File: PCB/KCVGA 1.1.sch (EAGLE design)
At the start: 61 parts, among them IC1 M68AW128MND, IC2 74245ADB, IC4 LD117AS12TR, IC5 LD117AS33TR, U1 XC3S50ATQ144, U2 PIC32MX250F128B_I_SS, U3 PIC32MX270F256D, X1 D-SUB15, X2 MINI-USB

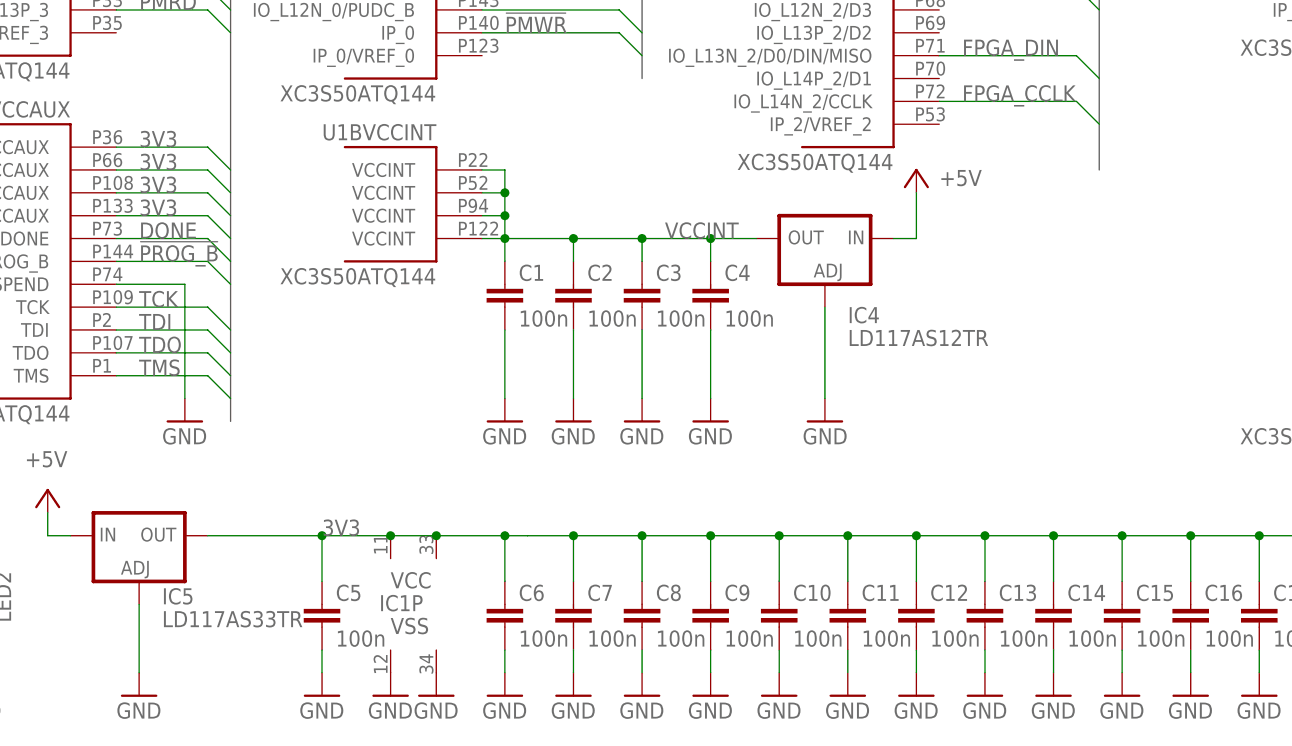
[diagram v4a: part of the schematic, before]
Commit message: added LDO output caps added Eagle3d files
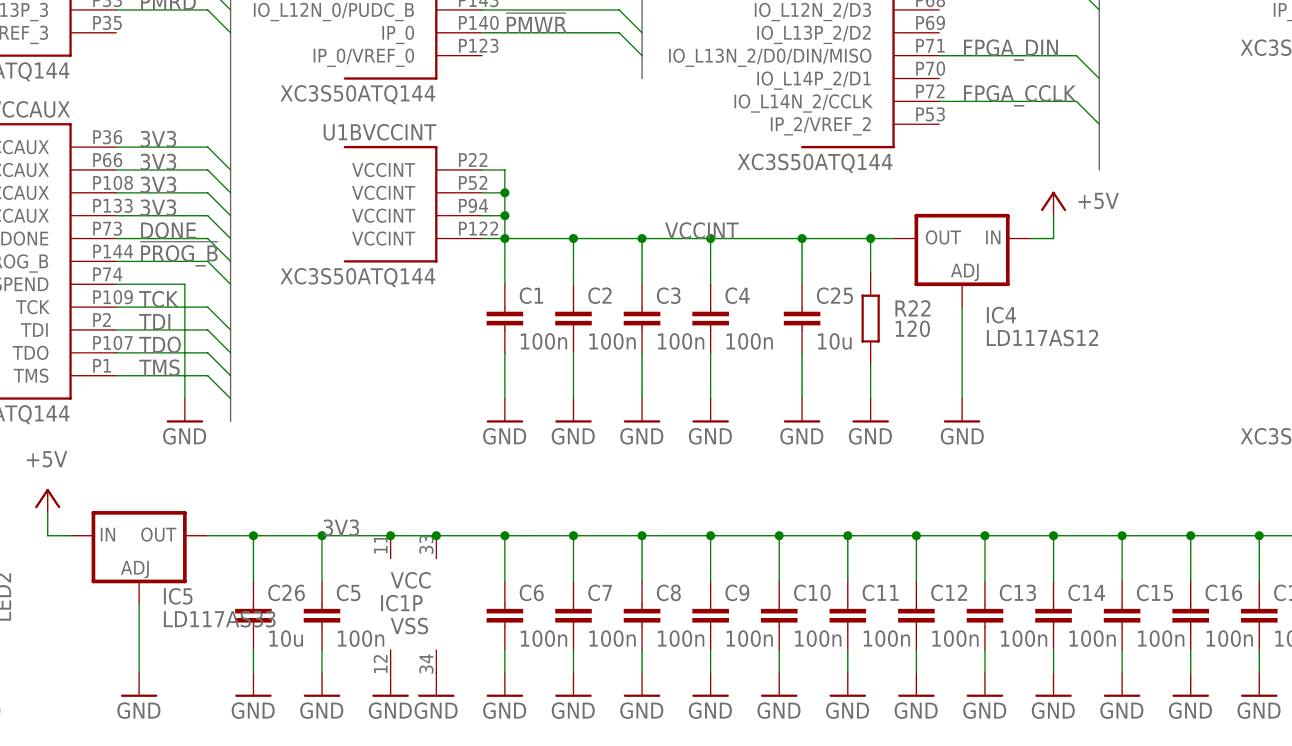
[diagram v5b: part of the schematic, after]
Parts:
- added C25, C26: 10u, rcl:C-EUC1206K
- added R22: 120, rcl:R-EU_R0603
- IC4: value LD117AS12TR -> LD117AS12
- IC5: value LD117AS33TR -> LD117AS33
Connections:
- net 3V3: now also C26.1
- net GND: now also C25.2, C26.2, R22.1
- net VCCINT: now also C25.1, R22.2
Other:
- moved on the sheet: C1, C2, C3, C4, IC4
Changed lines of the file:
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@@
 <part name="GND29" library="supply1" deviceset="GND" device=""/>
 <part name="JP3" library="pinhead" deviceset="PINHD-1X6" device=""/>
-<part name="IC4" library="v-reg" deviceset="LD117A?*" device="S" technology="12TR"/>
-<part name="IC5" library="v-reg" deviceset="LD117A?*" device="S" technology="33TR"/>
+<part name="IC4" library="v-reg" deviceset="LD117A?*" device="S" technology="12TR" value="LD117AS12"/>
+<part name="IC5" library="v-reg" deviceset="LD117A?*" device="S" technology="33TR" value="LD117AS33"/>
 <part name="JP2" library="pinhead" deviceset="PINHD-1X3" device=""/>
 <part name="P+2" library="supply1" deviceset="+5V" device=""/>
@@
 <part name="JP1" library="pinhead" deviceset="PINHD-1X6" device=""/>
 <part name="U3" library="PIC32MX270" deviceset="PIC32MX250F128D-I_PT" device="" value="PIC32MX270F256D"/>
+<part name="C25" library="rcl" deviceset="C-EU" device="C1206K" value="10u"/>
+<part name="C26" library="rcl" deviceset="C-EU" device="C1206K" value="10u"/>
+<part name="GND42" library="supply1" deviceset="GND" device=""/>
+<part name="GND43" library="supply1" deviceset="GND" device=""/>
+<part name="R22" library="rcl" deviceset="R-EU_" device="R0603" value="120"/>
+<part name="GND44" library="supply1" deviceset="GND" device=""/>
 </parts>
 <sheets>
@@
 <instance part="U1" gate="BVCCAUX" x="-5.08" y="-10.16"/>
 <instance part="U1" gate="BVCCINT" x="35.56" y="-2.54"/>
-<instance part="C1" gate="G$1" x="43.18" y="-12.7"/>
-<instance part="C2" gate="G$1" x="50.8" y="-12.7"/>
-<instance part="C3" gate="G$1" x="58.42" y="-12.7"/>
-<instance part="C4" gate="G$1" x="66.04" y="-12.7"/>
+<instance part="C1" gate="G$1" x="43.18" y="-15.24"/>
+<instance part="C2" gate="G$1" x="50.8" y="-15.24"/>
+<instance part="C3" gate="G$1" x="58.42" y="-15.24"/>
+<instance part="C4" gate="G$1" x="66.04" y="-15.24"/>
 <instance part="GND1" gate="1" x="43.18" y="-27.94"/>
 <instance part="GND2" gate="1" x="50.8" y="-27.94"/>
@@
 <instance part="GND29" gate="1" x="167.64" y="76.2"/>
 <instance part="JP3" gate="A" x="177.8" y="83.82"/>
-<instance part="IC4" gate="G$1" x="78.74" y="-7.62" smashed="yes" rot="MR0">
-<attribute name="NAME" x="81.28" y="-15.24" size="1.778" layer="95" rot="MR180"/>
-<attribute name="VALUE" x="81.28" y="-17.78" size="1.778" layer="96" rot="MR180"/>
+<instance part="IC4" gate="G$1" x="93.98" y="-7.62" smashed="yes" rot="MR0">
+<attribute name="NAME" x="96.52" y="-15.24" size="1.778" layer="95" rot="MR180"/>
+<attribute name="VALUE" x="96.52" y="-17.78" size="1.778" layer="96" rot="MR180"/>
 </instance>
 <instance part="IC5" gate="G$1" x="2.54" y="-40.64"/>
 <instance part="JP2" gate="A" x="182.88" y="116.84" rot="R180"/>
-<instance part="P+2" gate="1" x="88.9" y="0" smashed="yes" rot="MR0">
-<attribute name="VALUE" x="91.44" y="0" size="1.778" layer="96" rot="MR180"/>
-</instance>
-<instance part="GND30" gate="1" x="78.74" y="-27.94" rot="MR0"/>
+<instance part="P+2" gate="1" x="104.14" y="-2.54" smashed="yes" rot="MR0">
+<attribute name="VALUE" x="106.68" y="-2.54" size="1.778" layer="96" rot="MR180"/>
+</instance>
+<instance part="GND30" gate="1" x="93.98" y="-27.94" rot="MR0"/>
 <instance part="GND31" gate="1" x="2.54" y="-58.42"/>
 <instance part="P+3" gate="1" x="-7.62" y="-35.56" smashed="yes">
@@
 <instance part="JP1" gate="A" x="170.18" y="124.46"/>
 <instance part="U3" gate="A" x="-55.88" y="264.16"/>
+<instance part="C25" gate="G$1" x="76.2" y="-15.24" smashed="yes">
+<attribute name="NAME" x="77.724" y="-14.859" size="1.778" layer="95"/>
+<attribute name="VALUE" x="77.724" y="-19.939" size="1.778" layer="96"/>
+</instance>
+<instance part="C26" gate="G$1" x="15.24" y="-48.26" smashed="yes">
+<attribute name="NAME" x="16.764" y="-47.879" size="1.778" layer="95"/>
+<attribute name="VALUE" x="16.764" y="-52.959" size="1.778" layer="96"/>
+</instance>
+<instance part="GND42" gate="1" x="15.24" y="-58.42"/>
+<instance part="GND43" gate="1" x="76.2" y="-27.94"/>
+<instance part="R22" gate="G$1" x="83.82" y="-16.51" smashed="yes" rot="R90">
+<attribute name="NAME" x="86.36" y="-16.2814" size="1.778" layer="95"/>
+<attribute name="VALUE" x="86.36" y="-18.542" size="1.778" layer="96"/>
+</instance>
+<instance part="GND44" gate="1" x="83.82" y="-27.94"/>
 </instances>
 <busses>
@@
 <pinref part="C1" gate="G$1" pin="2"/>
 <pinref part="GND1" gate="1" pin="GND"/>
-<wire x1="43.18" y1="-17.78" x2="43.18" y2="-25.4" width="0.1524" layer="91"/>
+<wire x1="43.18" y1="-20.32" x2="43.18" y2="-25.4" width="0.1524" layer="91"/>
 </segment>
 <segment>
 <pinref part="C2" gate="G$1" pin="2"/>
 <pinref part="GND2" gate="1" pin="GND"/>
-<wire x1="50.8" y1="-17.78" x2="50.8" y2="-25.4" width="0.1524" layer="91"/>
+<wire x1="50.8" y1="-20.32" x2="50.8" y2="-25.4" width="0.1524" layer="91"/>
 </segment>
 <segment>
 <pinref part="C3" gate="G$1" pin="2"/>
 <pinref part="GND3" gate="1" pin="GND"/>
-<wire x1="58.42" y1="-17.78" x2="58.42" y2="-25.4" width="0.1524" layer="91"/>
+<wire x1="58.42" y1="-20.32" x2="58.42" y2="-25.4" width="0.1524" layer="91"/>
 </segment>
 <segment>
 <pinref part="C4" gate="G$1" pin="2"/>
 <pinref part="GND4" gate="1" pin="GND"/>
-<wire x1="66.04" y1="-17.78" x2="66.04" y2="-25.4" width="0.1524" layer="91"/>
+<wire x1="66.04" y1="-20.32" x2="66.04" y2="-25.4" width="0.1524" layer="91"/>
 </segment>
 <segment>
@@
 <pinref part="GND30" gate="1" pin="GND"/>
 <pinref part="IC4" gate="G$1" pin="ADJ"/>
-<wire x1="78.74" y1="-15.24" x2="78.74" y2="-25.4" width="0.1524" layer="91"/>
+<wire x1="93.98" y1="-15.24" x2="93.98" y2="-25.4" width="0.1524" layer="91"/>
 </segment>
 <segment>
@@
 <label x="149.86" y="127" size="1.778" layer="95"/>
 </segment>
+<segment>
+<pinref part="C26" gate="G$1" pin="2"/>
+<pinref part="GND42" gate="1" pin="GND"/>
+<wire x1="15.24" y1="-53.34" x2="15.24" y2="-55.88" width="0.1524" layer="91"/>
+</segment>
+<segment>
+<pinref part="C25" gate="G$1" pin="2"/>
+<pinref part="GND43" gate="1" pin="GND"/>
+<wire x1="76.2" y1="-20.32" x2="76.2" y2="-25.4" width="0.1524" layer="91"/>
+</segment>
+<segment>
+<pinref part="R22" gate="G$1" pin="1"/>
+<pinref part="GND44" gate="1" pin="GND"/>
+<wire x1="83.82" y1="-21.59" x2="83.82" y2="-25.4" width="0.1524" layer="91"/>
+</segment>
 </net>
 <net name="VCCINT" class="0">
@@
 <wire x1="40.64" y1="0" x2="43.18" y2="0" width="0.1524" layer="91"/>
 <pinref part="C1" gate="G$1" pin="1"/>
-<wire x1="43.18" y1="-10.16" x2="43.18" y2="-7.62" width="0.1524" layer="91"/>
+<wire x1="43.18" y1="-12.7" x2="43.18" y2="-7.62" width="0.1524" layer="91"/>
 <pinref part="U1" gate="BVCCINT" pin="VCCINT@3"/>
 <wire x1="40.64" y1="-7.62" x2="43.18" y2="-7.62" width="0.1524" layer="91"/>
@@
 <wire x1="50.8" y1="-7.62" x2="58.42" y2="-7.62" width="0.1524" layer="91"/>
 <wire x1="58.42" y1="-7.62" x2="66.04" y2="-7.62" width="0.1524" layer="91"/>
-<wire x1="66.04" y1="-7.62" x2="66.04" y2="-10.16" width="0.1524" layer="91"/>
+<wire x1="66.04" y1="-7.62" x2="66.04" y2="-12.7" width="0.1524" layer="91"/>
 <pinref part="C3" gate="G$1" pin="1"/>
-<wire x1="58.42" y1="-10.16" x2="58.42" y2="-7.62" width="0.1524" layer="91"/>
+<wire x1="58.42" y1="-12.7" x2="58.42" y2="-7.62" width="0.1524" layer="91"/>
 <junction x="58.42" y="-7.62"/>
 <pinref part="C2" gate="G$1" pin="1"/>
-<wire x1="50.8" y1="-10.16" x2="50.8" y2="-7.62" width="0.1524" layer="91"/>
+<wire x1="50.8" y1="-12.7" x2="50.8" y2="-7.62" width="0.1524" layer="91"/>
 <junction x="50.8" y="-7.62"/>
 <label x="60.96" y="-7.62" size="1.778" layer="95"/>
 <pinref part="IC4" gate="G$1" pin="OUT"/>
-<wire x1="71.12" y1="-7.62" x2="66.04" y2="-7.62" width="0.1524" layer="91"/>
+<wire x1="86.36" y1="-7.62" x2="83.82" y2="-7.62" width="0.1524" layer="91"/>
 <junction x="66.04" y="-7.62"/>
+<pinref part="C25" gate="G$1" pin="1"/>
+<wire x1="83.82" y1="-7.62" x2="76.2" y2="-7.62" width="0.1524" layer="91"/>
+<wire x1="76.2" y1="-7.62" x2="66.04" y2="-7.62" width="0.1524" layer="91"/>
+<wire x1="76.2" y1="-12.7" x2="76.2" y2="-7.62" width="0.1524" layer="91"/>
+<junction x="76.2" y="-7.62"/>
+<pinref part="R22" gate="G$1" pin="2"/>
+<wire x1="83.82" y1="-11.43" x2="83.82" y2="-7.62" width="0.1524" layer="91"/>
+<junction x="83.82" y="-7.62"/>
 </segment>
 </net>
@@
 <junction x="30.48" y="-40.64"/>
 <pinref part="IC5" gate="G$1" pin="OUT"/>
-<wire x1="10.16" y1="-40.64" x2="22.86" y2="-40.64" width="0.1524" layer="91"/>
+<wire x1="10.16" y1="-40.64" x2="15.24" y2="-40.64" width="0.1524" layer="91"/>
 <junction x="22.86" y="-40.64"/>
+<pinref part="C26" gate="G$1" pin="1"/>
+<wire x1="15.24" y1="-40.64" x2="22.86" y2="-40.64" width="0.1524" layer="91"/>
+<wire x1="15.24" y1="-45.72" x2="15.24" y2="-40.64" width="0.1524" layer="91"/>
+<junction x="15.24" y="-40.64"/>
 </segment>
 <segment>
@@
 <pinref part="P+2" gate="1" pin="+5V"/>
 <pinref part="IC4" gate="G$1" pin="IN"/>
-<wire x1="88.9" y1="-2.54" x2="88.9" y2="-7.62" width="0.1524" layer="91"/>
-<wire x1="88.9" y1="-7.62" x2="86.36" y2="-7.62" width="0.1524" layer="91"/>
-</segment>
-<segment>
+<wire x1="104.14" y1="-5.08" x2="104.14" y2="-7.62" width="0.1524" layer="91"/>
+<wire x1="104.14" y1="-7.62" x2="101.6" y2="-7.62" width="0.1524" layer="91"/>
+</segment>
+<segment>

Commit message: Finished silk screen
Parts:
- removed JP1: (no value), pinhead:PINHD-1X6
- removed JP2: (no value), pinhead:PINHD-1X3
- removed U1: XC3S50ATQ144, xilinx_devices_V6:XC3S50ATQ144
- removed U2: PIC32MX250F128B_I_SS, PIC32MX270:PIC32MX250F128B_I_SS
- removed U3: PIC32MX270F256D, PIC32MX270:PIC32MX250F128D-I_PT
- added IC3: M68AW128MND, st-microelectronics:M68AW128MND
- added IC6: 74245ADB, 74xx-eu:74245ADB
- added X3: MINI-USB, con-cypressindustries:MINI-USB-SCHIELD-32005-301
- added X4: (no value), jumper:JP6Q
- added X6: (no value), pinhead:PINHD-1X6
- C22: value 10u -> 100n; device rcl:C-EUC1206K -> rcl:C-EUC0603K
- C24: value 100n -> 10u; device rcl:C-EUC0603K -> rcl:C-EUC1206K
- IC1: value M68AW128MND -> XC3S50ATQ144; device st-microelectronics:M68AW128MND -> xilinx_devices_V6:XC3S50ATQ144
- IC2: value 74245ADB -> PIC32MX250F128; device 74xx-eu:74245ADB -> PIC32MX270:PIC32MX250F128B_I_SS
- X2: value MINI-USB -> (none); device con-cypressindustries:MINI-USB-SCHIELD-32005-301 -> pinhead:PINHD-1X3
- renumbered JP3 to X5, SV1 to X7
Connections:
- removed net FPGA_CLK: U1B0.IO_L07N_0/GCLK7, U2.OSC2/CLKO/RPA3/PMA0/RA3
- new net JP0: IC1B2.IO_L14P_2/D1, X4.2
- new net JP1: IC1B2.IO_L13P_2/D2, X4.4
- new net JP2: IC1B2.IO_L12N_2/D3, X4.6
- new net JP3: IC1B1.IO_L02P_1/LDC1, X4.8
- new net JP4: IC1B1.IO_L01P_1/HDC, X4.10
- new net JP5: IC1B1.IO_L02N_1/LDC0, X4.12
- net !BHE: now also IC1B3.IO_L03P_3, IC3G$1.!UB; no longer IC1G$1.!UB, U1B3.IO_L03P_3
- net !BLE: now also IC1B3.IO_L03N_3, IC3G$1.!LB; no longer IC1G$1.!LB, U1B3.IO_L03N_3
- net !CE: now also IC1B1.IO_L09P_1, IC3G$1.!E; no longer IC1G$1.!E, U1B1.IO_L09P_1
- net !FPGA_RESET: now also IC1B3.IO_L08P_3/TRDY2/LHCLK6, IC2.OSC2/CLKO/RPA3/PMA0/RA3; no longer U1B3.IO_L08P_3/TRDY2/LHCLK6
- net !INIT_B: now also IC1B2.IO_L12P_2/INIT_B, IC2.TMS/RPB5/USBID/RB5; no longer U1B2.IO_L12P_2/INIT_B, U2.TMS/RPB5/USBID/RB5
- net !OE: now also IC1B3.IO_L01N_3, IC3G$1.!G; no longer IC1G$1.!G, U1B3.IO_L01N_3
- net !PMRD: now also IC1B3.IP_L13P_3, IC2.AN11/RPB13/CTPLS/PMRD/RB13; no longer U1B3.IP_L13P_3, U2.AN11/RPB13/CTPLS/PMRD/RB13
- net !PMWR: now also IC1B0.IP_0, IC2.AN5/C1INA/C2INC/RTCC/RPB3/SCL2/PMWR/RB3; no longer U1B0.IP_0, U2.AN5/C1INA/C2INC/RTCC/RPB3/SCL2/PMWR/RB3
- net !PROG_B: now also IC1BVCCAUX.PROG_B, IC2.SOSCI/RPB4/RB4; no longer U1BVCCAUX.PROG_B, U2.SOSCI/RPB4/RB4
- net !RESET: now also IC2.MCLR, X6.1; no longer JP1.1, U2.MCLR
- net !WE: now also IC1B1.IO_L04N_1/RHCLK1, IC3G$1.!W; no longer IC1G$1.!W, U1B1.IO_L04N_1/RHCLK1
- net +5V: now also C22.1, X2.2; no longer C24.1, JP2.2
- net 3V3: now also IC1B0.IO_L12N_0/PUDC_B, IC1B0.VCCO_0@0, IC1B0.VCCO_0@1, IC1B1.VCCO_1@0, IC1B1.VCCO_1@1, IC1B2.IO_L01N_2/M0, IC1B2.IO_L01P_2/M1, IC1B2.IO_L02P_2/M2, IC1B2.VCCO_2@0, IC1B2.VCCO_2@1, IC1B3.VCCO_3@0, IC1B3.VCCO_3@1, IC1BVCCAUX.VCCAUX@0, IC1BVCCAUX.VCCAUX@1, IC1BVCCAUX.VCCAUX@2, IC1BVCCAUX.VCCAUX@3, IC2.AVDD, IC2.VDD, IC2.VUSB3V3, IC3P.VCC@1, IC3P.VCC@2, IC6A.DIR, IC6P.VCC, X6.2; no longer IC1P.VCC@1, IC1P.VCC@2, IC2A.DIR, IC2P.VCC, JP1.2, U1B0.IO_L12N_0/PUDC_B, U1B0.VCCO_0@0, U1B0.VCCO_0@1, U1B1.VCCO_1@0, U1B1.VCCO_1@1, U1B2.IO_L01N_2/M0, U1B2.IO_L01P_2/M1, U1B2.IO_L02P_2/M2, U1B2.VCCO_2@0, U1B2.VCCO_2@1, U1B3.VCCO_3@0, U1B3.VCCO_3@1, U1BVCCAUX.VCCAUX@0, U1BVCCAUX.VCCAUX@1, U1BVCCAUX.VCCAUX@2, U1BVCCAUX.VCCAUX@3, U2.AVDD, U2.VDD, U2.VUSB3V3
- net A0: now also IC1B1.IO_L09N_1, IC3G$1.A0; no longer IC1G$1.A0, U1B1.IO_L09N_1
- net A1: now also IC1B1.IO_L10P_1, IC3G$1.A1; no longer IC1G$1.A1, U1B1.IO_L10P_1
- net A10: now also IC1B3.IO_L12P_3, IC3G$1.A10; no longer IC1G$1.A10, U1B3.IO_L12P_3
- net A11: now also IC1B3.IO_L12N_3, IC3G$1.A11; no longer IC1G$1.A11, U1B3.IO_L12N_3
- net A12: now also IC1B1.IO_L01N_1/LDC2, IC3G$1.A12; no longer IC1G$1.A12, U1B1.IO_L01N_1/LDC2
- net A13: now also IC1B1.IO_1, IC3G$1.A13; no longer IC1G$1.A13, U1B1.IO_1
- net A14: now also IC1B1.IO_L03P_1, IC3G$1.A14; no longer IC1G$1.A14, U1B1.IO_L03P_1
- net A15: now also IC1B1.IO_L04P_1/RHCLK0, IC3G$1.A15; no longer IC1G$1.A15, U1B1.IO_L04P_1/RHCLK0
- net A16: now also IC1B1.IO_L03N_1, IC3G$1.A16; no longer IC1G$1.A16, U1B1.IO_L03N_1
- net A2: now also IC1B1.IO_L11P_1, IC3G$1.A2; no longer IC1G$1.A2, U1B1.IO_L11P_1
- net A3: now also IC1B1.IO_L10N_1, IC3G$1.A3; no longer IC1G$1.A3, U1B1.IO_L10N_1
- net A4: now also IC1B1.IO_L11N_1, IC3G$1.A4; no longer IC1G$1.A4, U1B1.IO_L11N_1
- net A5: now also IC1B3.IO_L02P_3, IC3G$1.A5; no longer IC1G$1.A5, U1B3.IO_L02P_3
- net A6: now also IC1B3.IO_L01P_3, IC3G$1.A6; no longer IC1G$1.A6, U1B3.IO_L01P_3
- net A7: now also IC1B3.IO_L02N_3, IC3G$1.A7; no longer IC1G$1.A7, U1B3.IO_L02N_3
- net A8: now also IC1B3.IO_L10N_3, IC3G$1.A8; no longer IC1G$1.A8, U1B3.IO_L10N_3
- net A9: now also IC1B3.IO_L11N_3, IC3G$1.A9; no longer IC1G$1.A9, U1B3.IO_L11N_3
- net CLK_32M: now also IC1B0.IO_L07N_0/GCLK7, IC2.OSC1/CLKI/RPA2/RA2; no longer U2.OSC1/CLKI/RPA2/RA2
- net D0: now also IC1B1.IO_L08N_1, IC3G$1.D0; no longer IC1G$1.D0, U1B1.IO_L08N_1
- net D1: now also IC1B1.IO_L08P_1, IC3G$1.D1; no longer IC1G$1.D1, U1B1.IO_L08P_1
- net D10: now also IC1B3.IO_L08N_3/LHCLK7, IC3G$1.D10; no longer IC1G$1.D10, U1B3.IO_L08N_3/LHCLK7
- net D11: now also IC1B3.IO_L07N_3/LHCLK5, IC3G$1.D11; no longer IC1G$1.D11, U1B3.IO_L07N_3/LHCLK5
- net D12: now also IC1B3.IO_L06P_3/LHCLK2, IC3G$1.D12; no longer IC1G$1.D12, U1B3.IO_L06P_3/LHCLK2
- net D13: now also IC1B3.IO_L05N_3/LHCLK1, IC3G$1.D13; no longer IC1G$1.D13, U1B3.IO_L05N_3/LHCLK1
- net D14: now also IC1B3.IO_L05P_3/LHCLK0, IC3G$1.D14; no longer IC1G$1.D14, U1B3.IO_L05P_3/LHCLK0
- net D15: now also IC1B3.IO_L04P_3, IC3G$1.D15; no longer IC1G$1.D15, U1B3.IO_L04P_3
- net D2: now also IC1B1.IO_L07N_1/RHCLK7, IC3G$1.D2; no longer IC1G$1.D2, U1B1.IO_L07N_1/RHCLK7
- net D3: now also IC1B1.IO_L06N_1/RHCLK5, IC3G$1.D3; no longer IC1G$1.D3, U1B1.IO_L06N_1/RHCLK5
- net D4: now also IC1B1.IO_L07P_1/IRDY1/RHCLK6, IC3G$1.D4; no longer IC1G$1.D4, U1B1.IO_L07P_1/IRDY1/RHCLK6
- net D5: now also IC1B1.IO_L06P_1/RHCLK4, IC3G$1.D5; no longer IC1G$1.D5, U1B1.IO_L06P_1/RHCLK4
- net D6: now also IC1B1.IO_L05N_1/TRDY1/RHCLK3, IC3G$1.D6; no longer IC1G$1.D6, U1B1.IO_L05N_1/TRDY1/RHCLK3
- net D7: now also IC1B1.IO_L05P_1/RHCLK2, IC3G$1.D7; no longer IC1G$1.D7, U1B1.IO_L05P_1/RHCLK2
- net D8: now also IC1B3.IO_L09N_3, IC3G$1.D8; no longer IC1G$1.D8, U1B3.IO_L09N_3
- net D9: now also IC1B3.IO_L09P_3, IC3G$1.D9; no longer IC1G$1.D9, U1B3.IO_L09P_3
- net DONE: now also IC1BVCCAUX.DONE; no longer U1BVCCAUX.DONE
- net FPGA_CCLK: now also IC1B2.IO_L14N_2/CCLK, IC2.CVREF/AN10/C3INB/RPB14/VBUSON/SCK1/CTED5/RB14; no longer U1B2.IO_L14N_2/CCLK, U2.CVREF/AN10/C3INB/RPB14/VBUSON/SCK1/CTED5/RB14
- net FPGA_DIN: now also IC1B2.IO_L13N_2/D0/DIN/MISO, IC2.SOSCO/RPA4/T1CK/CTED9/PMA1/RA4; no longer U1B2.IO_L13N_2/D0/DIN/MISO, U2.SOSCO/RPA4/T1CK/CTED9/PMA1/RA4
- net GND: now also IC1BGND.GND@0, IC1BGND.GND@1, IC1BGND.GND@10, IC1BGND.GND@11, IC1BGND.GND@12, IC1BGND.GND@2, IC1BGND.GND@3, IC1BGND.GND@4, IC1BGND.GND@5, IC1BGND.GND@6, IC1BGND.GND@7, IC1BGND.GND@8, IC1BGND.GND@9, IC1BVCCAUX.SUSPEND, IC2.AVSS, IC2.VSS, IC2.VSS_2, IC3P.VSS@1, IC3P.VSS@2, IC6A.G, IC6P.GND, X3G$1.5, X3S.S1, X3S.S2, X3S.S3, X3S.S4, X4.1, X4.11, X4.3, X4.5, X4.7, X4.9, X6.3; no longer IC1P.VSS@1, IC1P.VSS@2, IC2A.G, IC2P.GND, JP1.3, U1BGND.GND@0, U1BGND.GND@1, U1BGND.GND@10, U1BGND.GND@11, U1BGND.GND@12, U1BGND.GND@2, U1BGND.GND@3, U1BGND.GND@4, U1BGND.GND@5, U1BGND.GND@6, U1BGND.GND@7, U1BGND.GND@8, U1BGND.GND@9, U1BVCCAUX.SUSPEND, U2.AVSS, U2.VSS, U2.VSS_2, X2G$1.5, X2S.S1, X2S.S2, X2S.S3, X2S.S4
- net KC_B: now also IC1B0.IO_L09N_0/GCLK11, IC6A.A3; no longer IC2A.A3, U1B0.IO_L09N_0/GCLK11
- net KC_CLK: now also IC1B0.IO_0, IC6A.A8; no longer IC2A.A8, U1B0.IO_0
- net KC_EX: now also IC1B0.IO_L08N_0/GCLK9, IC6A.A2; no longer IC2A.A2, U1B0.IO_L08N_0/GCLK9
- net KC_EZ: now also IC1B0.IO_L09P_0/GCLK10, IC6A.A1; no longer IC2A.A1, U1B0.IO_L09P_0/GCLK10
- net KC_G: now also IC1B0.IO_L10P_0, IC6A.A4; no longer IC2A.A4, U1B0.IO_L10P_0
- net KC_HSYNC: now also IC1B0.IO_L11N_0, IC6A.A7; no longer IC2A.A7, U1B0.IO_L11N_0
- net KC_R: now also IC1B0.IO_L10N_0, IC6A.A5; no longer IC2A.A5, U1B0.IO_L10N_0
- net KC_VSYNC: now also IC1B0.IO_L11P_0, IC6A.A6; no longer IC2A.A6, U1B0.IO_L11P_0
- net N$1: now also IC2.VBUS, X2.3, X3G$1.1; no longer JP2.3, U2.VBUS, X2G$1.1
- net N$11: now also IC2.PGEC2/RPB11/D-/RB11; no longer U2.PGEC2/RPB11/D-/RB11
- net N$12: now also IC2.PGED2/RPB10/D+/CTED11/RB10; no longer U2.PGED2/RPB10/D+/CTED11/RB10
- net N$13: now also X3G$1.2; no longer X2G$1.2
- net N$14: now also X3G$1.3; no longer X2G$1.3
- net N$16: now also C24.1, IC2.VCAP; no longer C22.1, U2.VCAP
- net N$2: now also IC6A.B1; no longer IC2A.B1
- net N$20: now also X2.1; no longer JP2.1
- net N$22: now also IC2.AN9/C3INA/RPB15/SCK2/CTED6/PMCS1/RB15; no longer U2.AN9/C3INA/RPB15/SCK2/CTED6/PMCS1/RB15
- net N$3: now also IC6A.B2; no longer IC2A.B2
- net N$4: now also IC6A.B3; no longer IC2A.B3
- net N$5: now also IC6A.B4; no longer IC2A.B4
- net N$6: now also IC6A.B5; no longer IC2A.B5
- net N$7: now also IC6A.B6; no longer IC2A.B6
- net N$8: now also IC6A.B7; no longer IC2A.B7
- net N$9: now also IC6A.B8; no longer IC2A.B8
- net PMD0: now also IC1B2.IO_L04P_2/VS2, IC2.PGED1/AN2/C1IND/C2INB/C3IND/RPB0/PMD0/RB0, X6.4; no longer JP1.4, U1B2.IO_L04P_2/VS2, U2.PGED1/AN2/C1IND/C2INB/C3IND/RPB0/PMD0/RB0
- net PMD1: now also IC1B2.IO_L03N_2/VS1, IC2.PGEC1/AN3/C1INC/C2INA/RPB1/CTED12/PMD1/RB1, X6.5; no longer JP1.5, U1B2.IO_L03N_2/VS1, U2.PGEC1/AN3/C1INC/C2INA/RPB1/CTED12/PMD1/RB1
- net PMD2: now also IC1B2.IO_L04N_2/VS0, IC2.AN4/C1INB/C2IND/RPB2/SDA2/CTED13/PMD2/RB2; no longer U1B2.IO_L04N_2/VS0, U2.AN4/C1INB/C2IND/RPB2/SDA2/CTED13/PMD2/RB2
- net PMD3: now also IC1B3.IO_L10P_3, IC2.TDO/RPB9/SDA1/CTED4/PMD3/RB9; no longer U1B3.IO_L10P_3, U2.TDO/RPB9/SDA1/CTED4/PMD3/RB9
- net PMD4: now also IC1B3.IO_L11P_3, IC2.TCK/RPB8/SCL1/CTED10/PMD4/RB8; no longer U1B3.IO_L11P_3, U2.TCK/RPB8/SCL1/CTED10/PMD4/RB8
- net PMD5: now also IC1B3.IO_L07P_3/LHCLK4, IC2.TDI/RPB7/CTED3/PMD5/INT0/RB7; no longer U1B3.IO_L07P_3/LHCLK4, U2.TDI/RPB7/CTED3/PMD5/INT0/RB7
- net PMD6: now also IC1B2.IO_L03P_2/RDWR_B, IC2.PGEC3/VREF-/CVREF-/AN1/RPA1/CTED2/PMD6/RA1; no longer U1B2.IO_L03P_2/RDWR_B, U2.PGEC3/VREF-/CVREF-/AN1/RPA1/CTED2/PMD6/RA1
- net PMD7: now also IC1B2.IO_L02N_2/CSO_B, IC2.PGED3/VREF+/CVREF+/AN0/C3INC/RPA0/CTED1/PMD7/RA0; no longer U1B2.IO_L02N_2/CSO_B, U2.PGED3/VREF+/CVREF+/AN0/C3INC/RPA0/CTED1/PMD7/RA0
- net TCK: now also IC1BVCCAUX.TCK; no longer U1BVCCAUX.TCK
- net TDI: now also IC1BVCCAUX.TDI; no longer U1BVCCAUX.TDI
- net TDO: now also IC1BVCCAUX.TDO; no longer U1BVCCAUX.TDO
- net TMS: now also IC1BVCCAUX.TMS; no longer U1BVCCAUX.TMS
- net VCCINT: now also IC1BVCCINT.VCCINT@0, IC1BVCCINT.VCCINT@1, IC1BVCCINT.VCCINT@2, IC1BVCCINT.VCCINT@3; no longer U1BVCCINT.VCCINT@0, U1BVCCINT.VCCINT@1, U1BVCCINT.VCCINT@2, U1BVCCINT.VCCINT@3
- net VGA_B0: now also IC1B2.IO_L05P_2; no longer U1B2.IO_L05P_2
- net VGA_B1: now also IC1B2.IO_L06P_2; no longer U1B2.IO_L06P_2
- net VGA_B2: now also IC1B2.IO_L05N_2/D7; no longer U1B2.IO_L05N_2/D7
- net VGA_B3: now also IC1B2.IO_L06N_2/D6; no longer U1B2.IO_L06N_2/D6
- net VGA_G0: now also IC1B2.IO_L07P_2/D5; no longer U1B2.IO_L07P_2/D5
- net VGA_G1: now also IC1B2.IO_L07N_2/D4; no longer U1B2.IO_L07N_2/D4
- net VGA_G2: now also IC1B2.IO_L08P_2/GCLK14; no longer U1B2.IO_L08P_2/GCLK14
- net VGA_G3: now also IC1B2.IO_L08N_2/GCLK15; no longer U1B2.IO_L08N_2/GCLK15
- net VGA_HSYNC: now also IC1B2.IO_L11N_2/DOUT; no longer U1B2.IO_L11N_2/DOUT
- net VGA_R0: now also IC1B2.IO_L09P_2/GCLK0; no longer U1B2.IO_L09P_2/GCLK0
- net VGA_R1: now also IC1B2.IO_L10P_2/GCLK2; no longer U1B2.IO_L10P_2/GCLK2
- net VGA_R2: now also IC1B2.IO_L09N_2/GCLK1; no longer U1B2.IO_L09N_2/GCLK1
- net VGA_R3: now also IC1B2.IO_L10N_2/GCLK3; no longer U1B2.IO_L10N_2/GCLK3
- net VGA_VSYNC: now also IC1B2.IO_2/MOSI/CSI_B; no longer U1B2.IO_2/MOSI/CSI_B
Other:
- note removed: "TODO: !FPGA_RESET, FPGA-Jumper"
- moved on the sheet: C21, C22, C23, C24, R17, XO1
